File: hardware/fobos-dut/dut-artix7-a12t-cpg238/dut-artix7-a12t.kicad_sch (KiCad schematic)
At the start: 4 parts

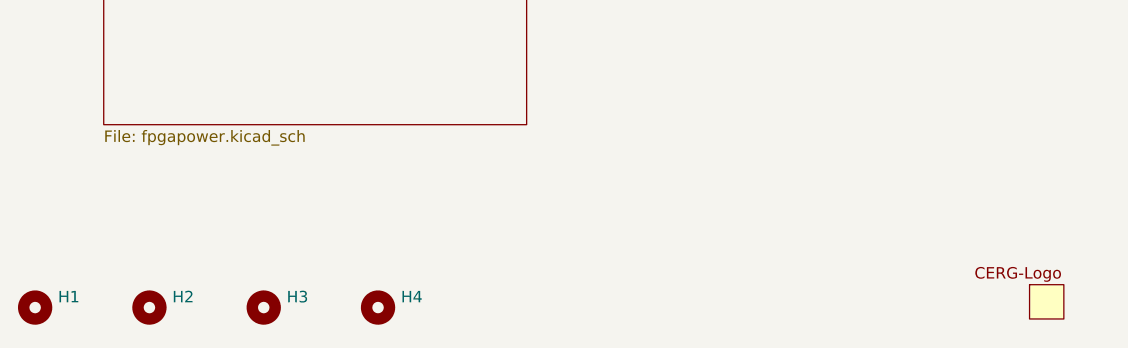
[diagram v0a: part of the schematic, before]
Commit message: transitioned artix-7 dut to Kikad 6
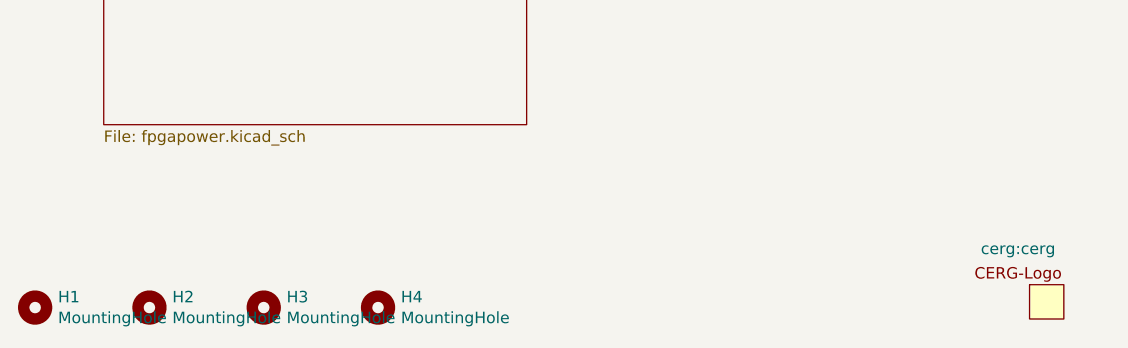
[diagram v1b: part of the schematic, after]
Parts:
- H1, H2, H3, H4: value (none) -> MountingHole; footprint (none) -> cerg:MH_4-40
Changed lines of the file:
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@@
       (effects (font (size 1.27 1.27)) (justify left))
     )
-    (property "Value" "" (id 1) (at 34.29 190.373 0)
+    (property "Value" "MountingHole" (id 1) (at 34.29 190.373 0)
       (effects (font (size 1.27 1.27)) (justify left))
     )
-    (property "Footprint" "" (id 2) (at 31.75 189.23 0)
+    (property "Footprint" "cerg:MH_4-40" (id 2) (at 31.75 189.23 0)
       (effects (font (size 1.27 1.27)) hide)
     )
@@
       (effects (font (size 1.27 1.27)) (justify left))
     )
-    (property "Value" "" (id 1) (at 46.99 190.373 0)
+    (property "Value" "MountingHole" (id 1) (at 46.99 190.373 0)
       (effects (font (size 1.27 1.27)) (justify left))
     )
-    (property "Footprint" "" (id 2) (at 44.45 189.23 0)
+    (property "Footprint" "cerg:MH_4-40" (id 2) (at 44.45 189.23 0)
       (effects (font (size 1.27 1.27)) hide)
     )
@@
       (effects (font (size 1.27 1.27)) (justify left))
     )
-    (property "Value" "" (id 1) (at 59.69 190.373 0)
+    (property "Value" "MountingHole" (id 1) (at 59.69 190.373 0)
       (effects (font (size 1.27 1.27)) (justify left))
     )
-    (property "Footprint" "" (id 2) (at 57.15 189.23 0)
+    (property "Footprint" "cerg:MH_4-40" (id 2) (at 57.15 189.23 0)
       (effects (font (size 1.27 1.27)) hide)
     )
@@
       (effects (font (size 1.27 1.27)) (justify left))
     )
-    (property "Value" "" (id 1) (at 72.39 190.373 0)
+    (property "Value" "MountingHole" (id 1) (at 72.39 190.373 0)
       (effects (font (size 1.27 1.27)) (justify left))
     )
-    (property "Footprint" "" (id 2) (at 69.85 189.23 0)
+    (property "Footprint" "cerg:MH_4-40" (id 2) (at 69.85 189.23 0)
       (effects (font (size 1.27 1.27)) hide)
     )
@@
       (effects (font (size 1.27 1.27)) hide)
     )
-    (property "Value" "" (id 1) (at 140.97 192.405 0)
+    (property "Value" "CERG-logo" (id 1) (at 140.97 192.405 0)
       (effects (font (size 1.27 1.27)) hide)
     )
-    (property "Footprint" "" (id 2) (at 140.97 182.7022 0))
+    (property "Footprint" "cerg:cerg" (id 2) (at 140.97 182.7022 0))
     (property "Datasheet" "" (id 3) (at 140.97 179.705 0)
       (effects (font (size 1.27 1.27)) hide)
@@
       (reference "#PWR01") (unit 1) (value "+1V0") (footprint "")
     )
-    (path "/00000000-0000-0000-0000-00005f449901/00000000-0000-0000-0000-00005fdf12f8"
-      (reference "#PWR02") (unit 1) (value "+1V8") (footprint "")
-    )
     (path "/00000000-0000-0000-0000-00005f449901/00000000-0000-0000-0000-00005fda6ecc"
       (reference "#PWR03") (unit 1) (value "GND") (footprint "")
@@
       (reference "#PWR030") (unit 1) (value "GND") (footprint "")
     )
-    (path "/00000000-0000-0000-0000-00005f20da36/00000000-0000-0000-0000-000060abda54"
-      (reference "#PWR031") (unit 1) (value "+3.3V") (footprint "")
-    )
     (path "/00000000-0000-0000-0000-00005f3a1954/00000000-0000-0000-0000-000060e483db"
       (reference "#PWR032") (unit 1) (value "GND") (footprint "")
@@
       (reference "#PWR0149") (unit 1) (value "+3V3") (footprint "")
     )
+    (path "/00000000-0000-0000-0000-00005f3a1954/ab30a68f-61c3-425a-a43a-e9587a8eba62"
+      (reference "#PWR?") (unit 1) (value "GND") (footprint "")
+    )
+    (path "/00000000-0000-0000-0000-00005f449901/bb14f28a-4298-4a7c-a2f5-18a6242eef36"
+      (reference "#PWR?") (unit 1) (value "+5V") (footprint "")
+    )
+    (path "/00000000-0000-0000-0000-00005f3a1954/fc2d43f8-3212-4951-80b1-bd2e76ff15e7"
+      (reference "#PWR?") (unit 1) (value "GND") (footprint "")
+    )
     (path "/00000000-0000-0000-0000-00005f20da36/00000000-0000-0000-0000-00005f25f7b4"
       (reference "C1") (unit 1) (value "100nF") (footprint "Capacitor_SMD:C_0603_1608Metric")
@@
       (reference "D6") (unit 1) (value "LG_L29K-G2J1-24-Z") (footprint "LED_SMD:LED_0603_1608Metric")
     )
+    (path "/00000000-0000-0000-0000-00005f3a1954/4ed46b60-89b7-4efd-92cd-2249e78c622d"
+      (reference "D?") (unit 1) (value "LG_L29K-G2J1-24-Z") (footprint "LED_SMD:LED_0603_1608Metric")
+    )
+    (path "/00000000-0000-0000-0000-00005f3a1954/56aa51c5-7c47-43c4-846d-ff5dbc8d0cb3"
+      (reference "D?") (unit 1) (value "LG_L29K-G2J1-24-Z") (footprint "LED_SMD:LED_0603_1608Metric")
+    )
     (path "/00000000-0000-0000-0000-00005f449901/00000000-0000-0000-0000-00005f45a1d8"
       (reference "F1") (unit 1) (value "MF-MSMF050-2") (footprint "Fuse:Fuse_1206_3216Metric")
@@
     )
     (path "/00000000-0000-0000-0000-00005f449901/00000000-0000-0000-0000-00005f45a258"
-      (reference "JP3") (unit 1) (value "Shunt1R") (footprint "Connector_PinHeader_2.54mm:PinHeader_1x02_P2.54mm_Vertical")
+      (reference "JP3") (unit 1) (value "Shunt1V") (footprint "Connector_PinHeader_2.54mm:PinHeader_1x02_P2.54mm_Vertical")
     )
     (path "/00000000-0000-0000-0000-00005f20da36/00000000-0000-0000-0000-000060a66495"
       (reference "JP4") (unit 1) (value "FC3V3_3V3_SHUNT") (footprint "Connector_PinHeader_2.54mm:PinHeader_1x02_P2.54mm_Vertical")
     )
+    (path "/00000000-0000-0000-0000-00005f449901/611ccf95-8f44-486c-9362-081eda055810"
+      (reference "JP?") (unit 1) (value "Shunt1V8") (footprint "Connector_PinHeader_2.54mm:PinHeader_1x02_P2.54mm_Vertical")
+    )
+    (path "/00000000-0000-0000-0000-00005f449901/820a1c62-e7d6-4fd9-ab5a-a68226a0a5f3"
+      (reference "JP?") (unit 1) (value "Shunt3V3") (footprint "Connector_PinHeader_2.54mm:PinHeader_1x02_P2.54mm_Vertical")
+    )
     (path "/00000000-0000-0000-0000-00005f449901/00000000-0000-0000-0000-00005f45a1f7"
       (reference "L1") (unit 1) (value "1k/500mA") (footprint "Inductor_SMD:L_0603_1608Metric")
@@
       (reference "Q8") (unit 1) (value "MMBT3904") (footprint "Package_TO_SOT_SMD:SOT-23")
     )
+    (path "/00000000-0000-0000-0000-00005f3a1954/9d3f4056-22cc-4d70-bf3d-d716c6ab738e"
+      (reference "Q?") (unit 1) (value "BSS138") (footprint "Package_TO_SOT_SMD:SOT-23")
+    )
+    (path "/00000000-0000-0000-0000-00005f3a1954/ebf42449-f946-4d7c-a4cf-6566d4ce8993"
+      (reference "Q?") (unit 1) (value "BSS138") (footprint "Package_TO_SOT_SMD:SOT-23")
+    )
     (path "/00000000-0000-0000-0000-00005f20da36/00000000-0000-0000-0000-00005f245a18"
       (reference "R1") (unit 1) (value "22R") (footprint "Resistor_SMD:R_0603_1608Metric")
@@
     )
     (path "/00000000-0000-0000-0000-00005f449901/00000000-0000-0000-0000-00005fefac29"
-      (reference "R43") (unit 1) (value "10KR") (footprint "Resistor_SMD:R_0603_1608Metric")
+      (reference "R43") (unit 1) (value "30K") (footprint "Resistor_SMD:R_0603_1608Metric")
     )
     (path "/00000000-0000-0000-0000-00005f449901/00000000-0000-0000-0000-00005fefb18b"
-      (reference "R44") (unit 1) (value "10KR") (footprint "Resistor_SMD:R_0603_1608Metric")
+      (reference "R44") (unit 1) (value "150K") (footprint "Resistor_SMD:R_0603_1608Metric")
     )
     (path "/00000000-0000-0000-0000-00005f449901/00000000-0000-0000-0000-00005fefb44e"
-      (reference "R45") (unit 1) (value "10KR") (footprint "Resistor_SMD:R_0603_1608Metric")
+      (reference "R45") (unit 1) (value "180K") (footprint "Resistor_SMD:R_0603_1608Metric")
     )
     (path "/00000000-0000-0000-0000-00005f449901/00000000-0000-0000-0000-00005fefbe50"
@@
     )
     (path "/00000000-0000-0000-0000-00005f449901/00000000-0000-0000-0000-000060ba4ed6"
-      (reference "R75") (unit 1) (value "0.1R") (footprint "Resistor_SMD:R_0805_2012Metric_Pad1.20x1.40mm_HandSolder")
+      (reference "R75") (unit 1) (value "0R1") (footprint "Resistor_SMD:R_1206_3216Metric")
     )
     (path "/00000000-0000-0000-0000-00005f449901/00000000-0000-0000-0000-000060c1fb49"
-      (reference "R76") (unit 1) (value "0.1R") (footprint "Resistor_SMD:R_0805_2012Metric_Pad1.20x1.40mm_HandSolder")
+      (reference "R76") (unit 1) (value "0R1") (footprint "Resistor_SMD:R_1206_3216Metric")
     )
     (path "/00000000-0000-0000-0000-00005f22d594/00000000-0000-0000-0000-00006101fc56"
@@
       (reference "R78") (unit 1) (value "1KR") (footprint "Resistor_SMD:R_0603_1608Metric")
     )
+    (path "/00000000-0000-0000-0000-00005f3a1954/125dc889-8009-4161-b237-d444ab38af24"
+      (reference "R?") (unit 1) (value "10KR") (footprint "Resistor_SMD:R_0603_1608Metric")
+    )
+    (path "/00000000-0000-0000-0000-00005f3a1954/5a5519a2-56fc-4a1f-bbf6-4e9bc0e4f347"
+      (reference "R?") (unit 1) (value "800R") (footprint "Resistor_SMD:R_0603_1608Metric")
+    )
+    (path "/00000000-0000-0000-0000-00005f3a1954/97584d5e-8510-4122-a104-5e9683717e5a"
+      (reference "R?") (unit 1) (value "470R") (footprint "Resistor_SMD:R_0603_1608Metric")
+    )
+    (path "/00000000-0000-0000-0000-00005f3a1954/bcfabffc-94e7-4dec-bb59-8dd221d8f7a8"
+      (reference "R?") (unit 1) (value "100KR") (footprint "Resistor_SMD:R_0603_1608Metric")
+    )
     (path "/00000000-0000-0000-0000-00005f449901/00000000-0000-0000-0000-000060aff5c6"
       (reference "S1") (unit 1) (value "JS202011SCQN") (footprint "cerg:Switch_Slide_JS202011SCQN")
@@
       (reference "TP5") (unit 1) (value "5281") (footprint "cerg:5281")
     )
-    (path "/00000000-0000-0000-0000-00005f449901/00000000-0000-0000-0000-000060c21ab4"
-      (reference "TP6") (unit 1) (value "5281") (footprint "cerg:5281")
-    )
-    (path "/00000000-0000-0000-0000-00005f449901/00000000-0000-0000-0000-000060c22508"
-      (reference "TP7") (unit 1) (value "5281") (footprint "cerg:5281")
-    )
-    (path "/00000000-0000-0000-0000-00005f449901/00000000-0000-0000-0000-000060c1ff6e"
-      (reference "TP8") (unit 1) (value "5281") (footprint "cerg:5281")
-    )
-    (path "/00000000-0000-0000-0000-00005f449901/00000000-0000-0000-0000-000060c21fe1"
-      (reference "TP9") (unit 1) (value "5281") (footprint "cerg:5281")
-    )
     (path "/00000000-0000-0000-0000-000060d2f94f/00000000-0000-0000-0000-000060d317c1"
